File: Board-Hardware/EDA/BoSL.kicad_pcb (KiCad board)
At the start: 2 copper layers, 88 x 69.8 mm, 63 parts, among them CON1 Micro_SD_Card, CON2 BARREL_JACK, IC2 SIM7000, J1 Screw_Terminal_1x06, J2 Screw_Terminal_1x04, J3 Screw_Terminal_1x02, J4 Screw_Terminal_1x08, J5 Screw_Terminal_1x04, J6 RJ45, J7 USB_B_Micro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

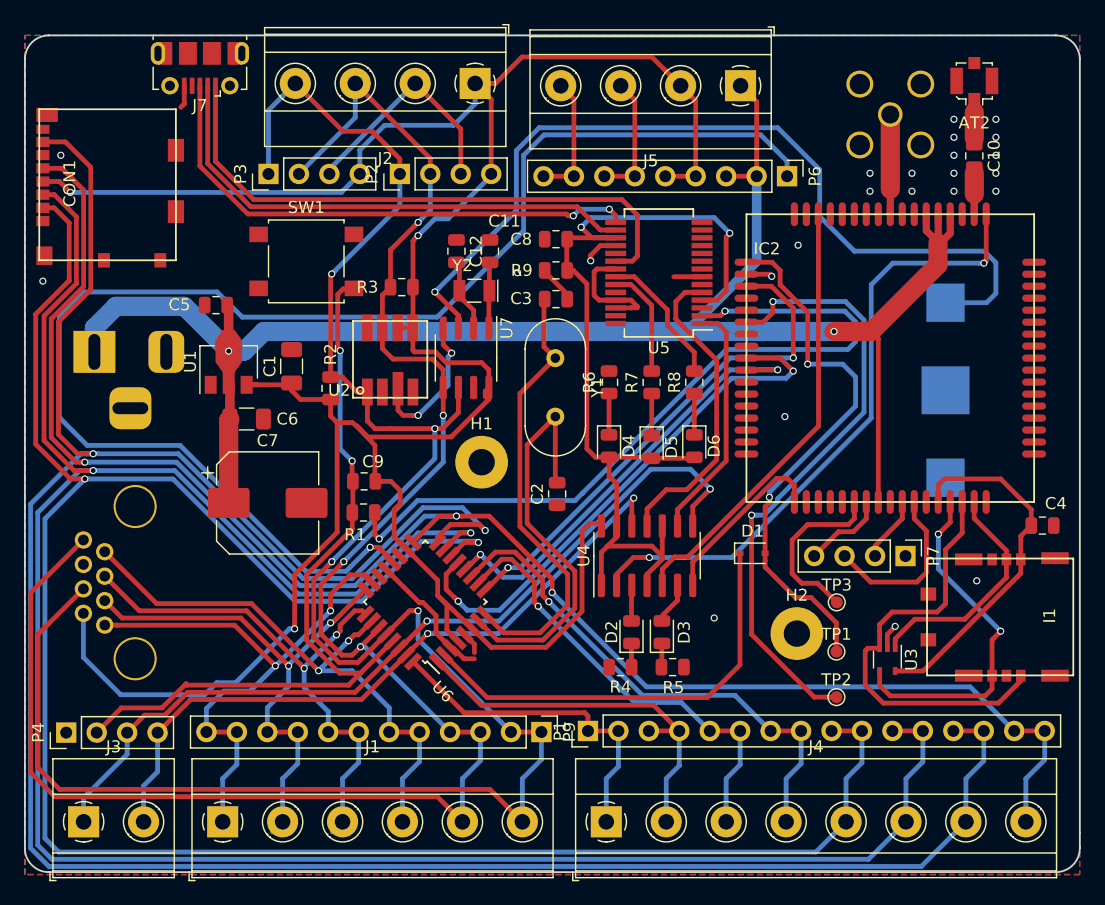
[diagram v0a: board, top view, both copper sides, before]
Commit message: added space savings of BoSL PCB
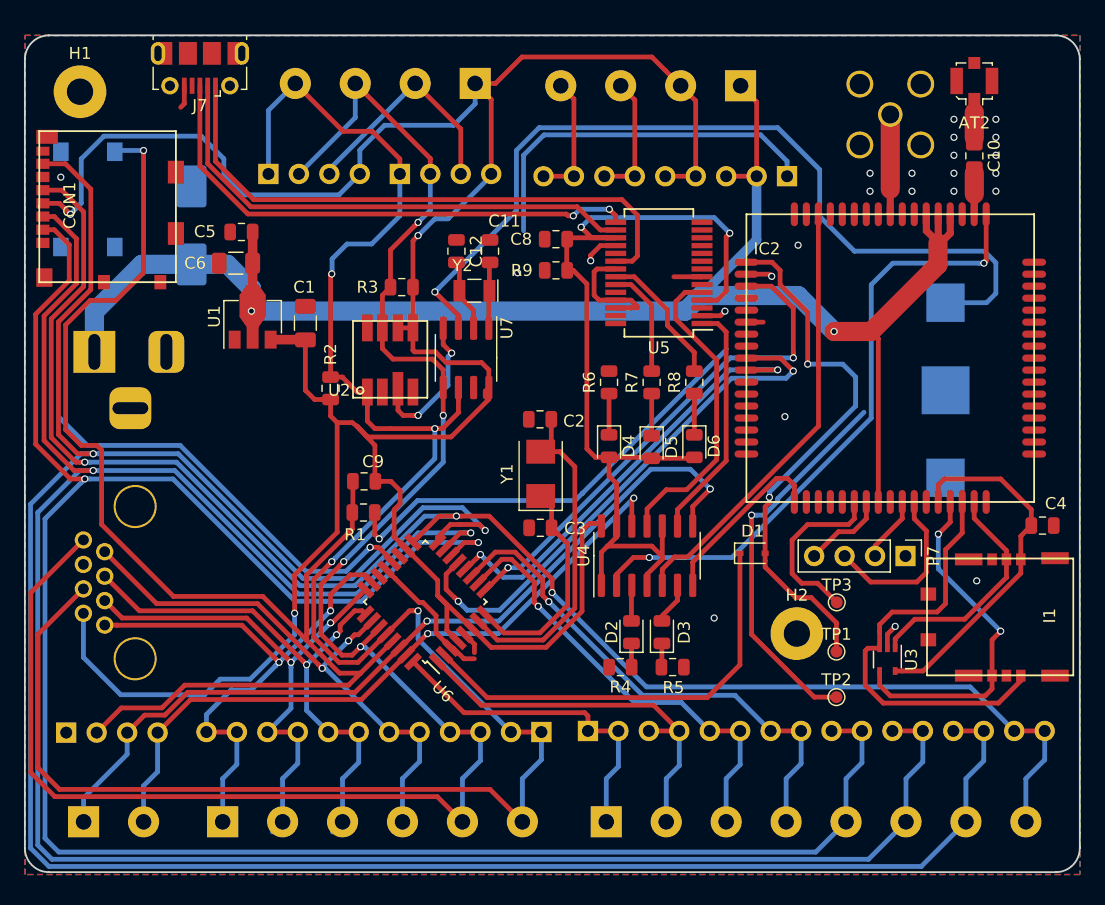
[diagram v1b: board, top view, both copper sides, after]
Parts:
- C7, J1, J2, J3, J4, J5, P1, P2, P3, P4, P6, P9, SW1: moved to B.Cu
- Y1: footprint Crystal:Crystal_HC49-4H_Vertical -> Crystal:Crystal_SMD_5032-2Pin_5.0x3.2mm
- moved H1 45.6 mm to (109.1, 67.7)
- moved C7 24.0 mm to (118.4, 78.8), turned to 90 degrees
- moved C3 19.1 mm to (147.5, 104.1), turned to 0 degrees
- moved SW1 18.9 mm to (109.8, 76.7), turned to 270 degrees
- moved C6 13.0 mm to (122.1, 82.0), turned to 180 degrees
- moved Y1 9.73 mm to (147.5, 99.6), turned to 90 degrees
- moved C5 6.46 mm to (122.6, 79.4)
- moved C2 6.39 mm to (147.5, 95.0), turned to 0 degrees
- moved U1 4.26 mm to (123.5, 86.9)
- moved C1 3.78 mm to (127.9, 87.0)
- moved CON1 1.83 mm to (105.7, 77.2)
- turned P1 to 270 degrees
- turned P2 to 270 degrees
- turned P3 to 270 degrees
- turned P4 to 270 degrees
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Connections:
- J7 pad 6: (no net) -> Net-(J7-Pad6)
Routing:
- net AREF: track 117.6 -> 65.7 mm
- net TLL_RST: track 66.2 -> 109.1 mm, vias 2 -> 1
- net Net-(C9-Pad2): track 63.9 -> 40.0 mm
- net Net-(C3-Pad2): track 37.4 -> 18.5 mm
- net Net-(IC2-Pad6): track 51.7 -> 33.7 mm, vias 2 -> 1
- net VPP: track 148.2 -> 135.2 mm
- net V_3.3: track 226.7 -> 236.1 mm
- net Net-(C2-Pad2): track 33.7 -> 28.1 mm
- net GND: track 106.0 -> 103.0 mm, vias 26 -> 25
- net SD_CS: track 180.0 -> 178.1 mm
- net SD_MOSI: track 187.9 -> 186.0 mm
- net SD_SCLK: track 137.7 -> 135.9 mm
- net SD_MISO: track 203.7 -> 201.9 mm
- net A3: track 48.0 -> 46.5 mm
- net SCL: track 173.7 -> 174.9 mm

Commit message: updated bosl with small screw terminals
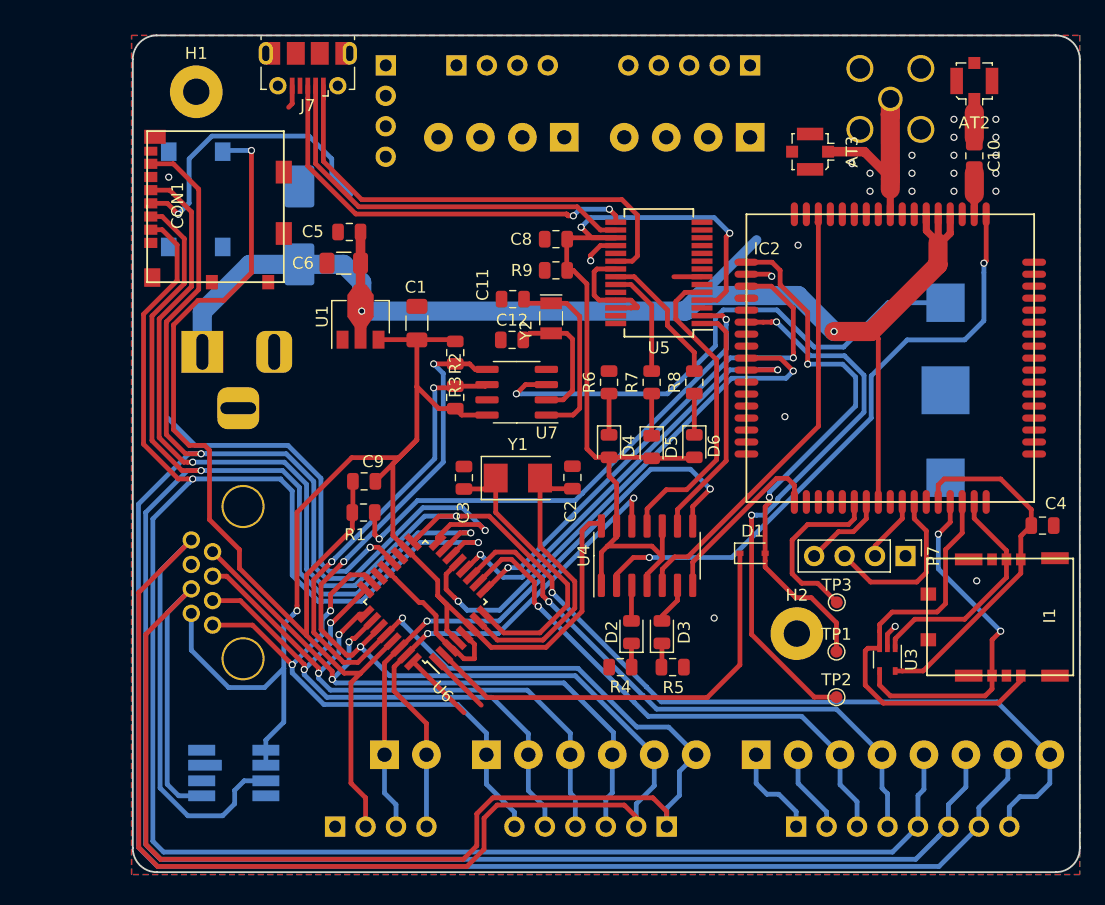
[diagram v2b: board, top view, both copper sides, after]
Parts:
- removed P1: CONN_01X16, Connector_PinHeader_2.54mm:PinHeader_1x16_P2.54mm_Vertical
- removed P6: CONN_01X09, Connector_PinHeader_2.54mm:PinHeader_1x09_P2.54mm_Vertical
- removed P9: CONN_01X12, Connector_PinHeader_2.54mm:PinHeader_1x12_P2.54mm_Vertical
- added AT3: AT-GNSS, Connector_Coaxial:U.FL_Molex_MCRF_73412-0110_Vertical, F.Cu at (170.0, 72.7)
- added J10: Conn_01x08, Connector_PinHeader_2.54mm:PinHeader_1x08_P2.54mm_Vertical, B.Cu at (168.8, 129.0)
- added J8: Conn_01x05, Connector_PinHeader_2.54mm:PinHeader_1x05_P2.54mm_Vertical, B.Cu at (165.0, 65.5)
- added J9: Conn_01x06, Connector_PinHeader_2.54mm:PinHeader_1x06_P2.54mm_Vertical, B.Cu at (158.0, 129.0)
- J1: footprint TerminalBlock_Phoenix:TerminalBlock_Phoenix_MKDS-1,5-6_1x06_P5.00mm_Horizontal -> TerminalBlock_Phoenix:TerminalBlock_Phoenix_PT-1,5-6-3.5-H_1x06_P3.50mm_Horizontal
- J2, J5: footprint TerminalBlock_Phoenix:TerminalBlock_Phoenix_MKDS-1,5-4_1x04_P5.00mm_Horizontal -> TerminalBlock_Phoenix:TerminalBlock_Phoenix_PT-1,5-4-3.5-H_1x04_P3.50mm_Horizontal
- J3: footprint TerminalBlock_Phoenix:TerminalBlock_Phoenix_MKDS-1,5-2_1x02_P5.00mm_Horizontal -> TerminalBlock_Phoenix:TerminalBlock_Phoenix_PT-1,5-2-3.5-H_1x02_P3.50mm_Horizontal
- J4: footprint TerminalBlock_Phoenix:TerminalBlock_Phoenix_MKDS-1,5-8_1x08_P5.00mm_Horizontal -> TerminalBlock_Phoenix:TerminalBlock_Phoenix_PT-1,5-8-3.5-H_1x08_P3.50mm_Horizontal
- U2: moved to B.Cu
- moved U2 36.9 mm to (122.0, 124.5), turned to 0 degrees
- moved J3 25.7 mm to (134.5, 123.0)
- moved P4 23.8 mm to (130.4, 129.0)
- moved J1 22.7 mm to (143.0, 123.0)
- moved P3 18.1 mm to (140.5, 65.5)
- moved J4 13.7 mm to (165.5, 123.0)
- moved R2 10.4 mm to (140.4, 93.2)
- moved H1 9.70 mm to (118.8, 67.7)
- moved C1 9.30 mm to (137.2, 87.0)
- moved P2 9.13 mm to (134.6, 65.5), turned to 180 degrees
- moved C5 9.00 mm to (131.6, 79.4)
- moved C6 9.00 mm to (131.1, 82.0)
- moved C7 9.00 mm to (127.4, 78.8)
- moved CON1 9.00 mm to (114.7, 77.2)
- moved CON2 9.00 mm to (119.3, 89.4)
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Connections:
- J5 pad 1: VPP -> GND
- J5 pad 2: V_3.3 -> VPP
- J5 pad 4: GND -> V_3.3
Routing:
- net V_3.3: track 236.1 -> 140.1 mm, vias 3 -> 2
- net GND: track 103.0 -> 50.3 mm, vias 25 -> 22
- net AREF: track 65.7 -> 29.7 mm
- net Net-(BT1-Pad1): track 73.3 -> 45.7 mm
- net SDA: track 154.5 -> 180.8 mm, vias 4 -> 3
- net VPP: track 135.2 -> 110.6 mm
- net D3: track 33.1 -> 12.1 mm
- net TLL_RST: track 109.1 -> 89.9 mm
- net TLL_RX: track 70.8 -> 52.1 mm
- net SD_MISO: track 201.9 -> 185.2 mm
- net TLL_TX: track 57.9 -> 42.4 mm
- net SD_MOSI: track 186.0 -> 171.4 mm
- net D2: track 28.3 -> 14.0 mm
- net Net-(IC2-Pad6): track 33.7 -> 47.0 mm, vias 1 -> 2
- net SD_CS: track 178.1 -> 165.7 mm
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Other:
- board size 88 x 69.8 mm -> 79 x 69.8 mm

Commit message: finished bosl rev0.4
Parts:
- J7: moved to B.Cu
- moved C1 4.66 mm to (135.4, 91.3), turned to 180 degrees
- turned J7 to 0 degrees
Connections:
- J7 pad 6: Net-(J7-Pad6) -> (no net)
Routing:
- net AREF: track 29.7 -> 99.2 mm
- net V_3.3: track 140.1 -> 196.9 mm, vias 2 -> 3
- net SCL: track 168.3 -> 204.6 mm, vias 3 -> 4
- net SDA: track 180.8 -> 216.5 mm, vias 3 -> 4
- net GND: track 50.3 -> 80.8 mm, vias 22 -> 30
- net D3: track 12.1 -> 40.3 mm
- net D2: track 14.0 -> 40.7 mm
- net VPP: track 110.6 -> 128.9 mm
- net SD_MISO: track 185.2 -> 179.4 mm
- net SD_SCLK: track 132.3 -> 135.0 mm
- net Net-(BT1-Pad1): track 45.7 -> 43.3 mm
- net USB_V: track 39.8 -> 41.8 mm, vias 0 -> 1
- net USB_DP: track 35.3 -> 33.5 mm, vias 2 -> 1
- net A3: track 54.6 -> 52.9 mm
- net A2: track 50.6 -> 49.4 mm
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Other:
- board text added: "D2"
- board text added: "D3"
- board text added: "RST"
- board text removed: "D8"
- board text removed: "D9"
- board text removed: "RESET"
